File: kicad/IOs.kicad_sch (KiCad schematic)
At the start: 57 parts, among them J1 Screw_Terminal_01x04, J2 Screw_Terminal_01x04, J3 Screw_Terminal_01x04, J4 Screw_Terminal_01x04, J5 Screw_Terminal_01x04, J6 Screw_Terminal_01x04, Q1 BSS306NH, Q2 BSS306NH, Q3 BSS306NH, Q4 BSS306NH, Q5 BSS306NH, Q6 BSS306NH, SW2 SW_Push, SW3 SW_Push, SW4 SW_Push, U1 IX4340NE, U2 IX4340NE, U3 IX4340NE

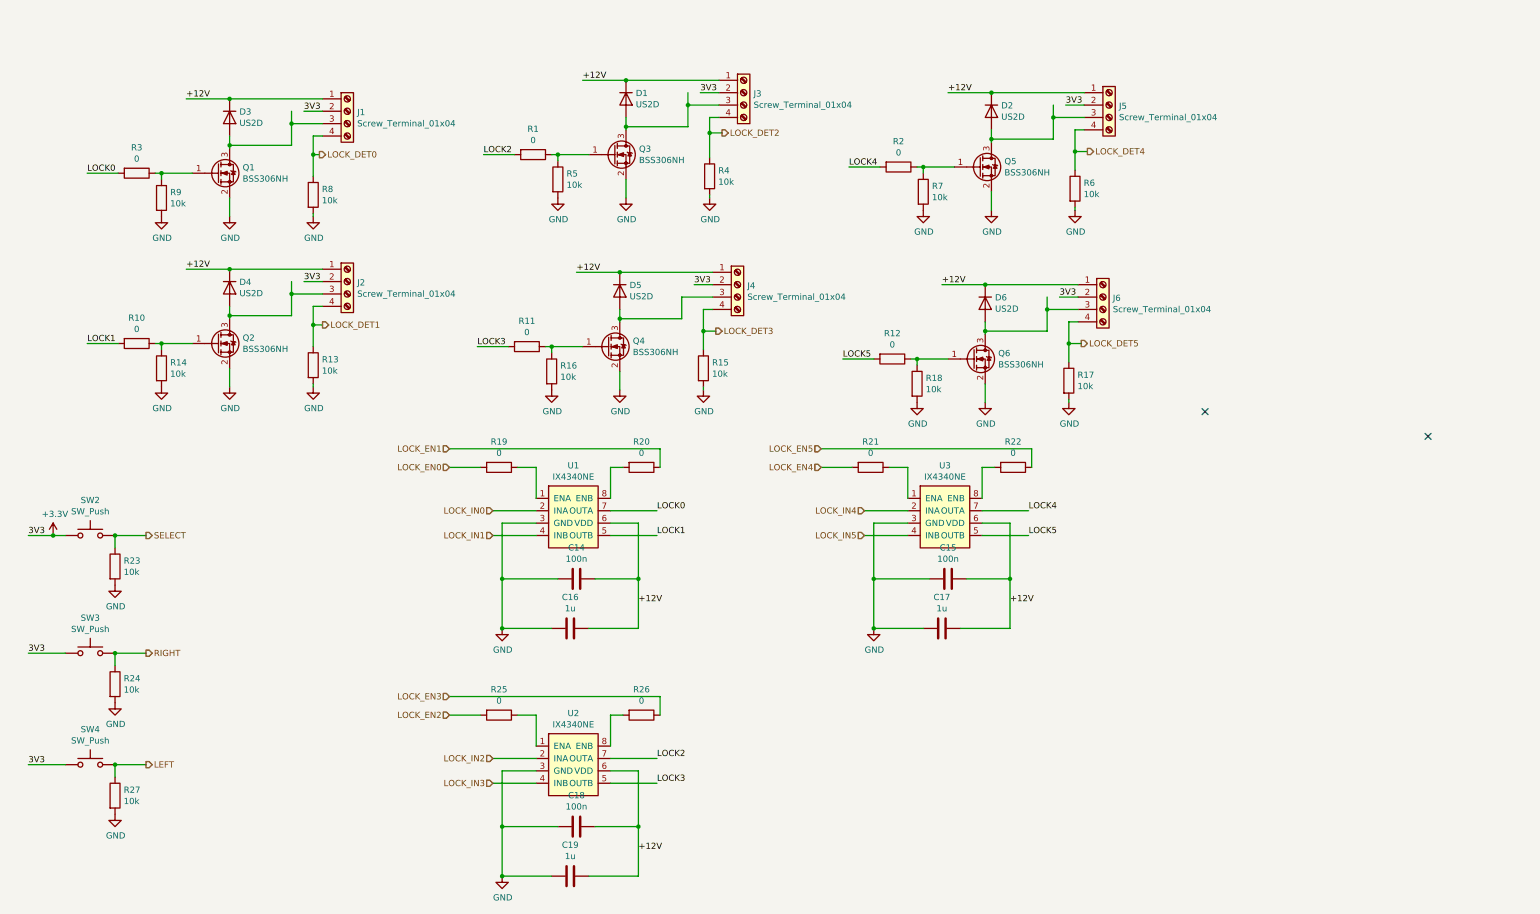
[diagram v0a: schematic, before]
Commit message: Update PCB with IO expander
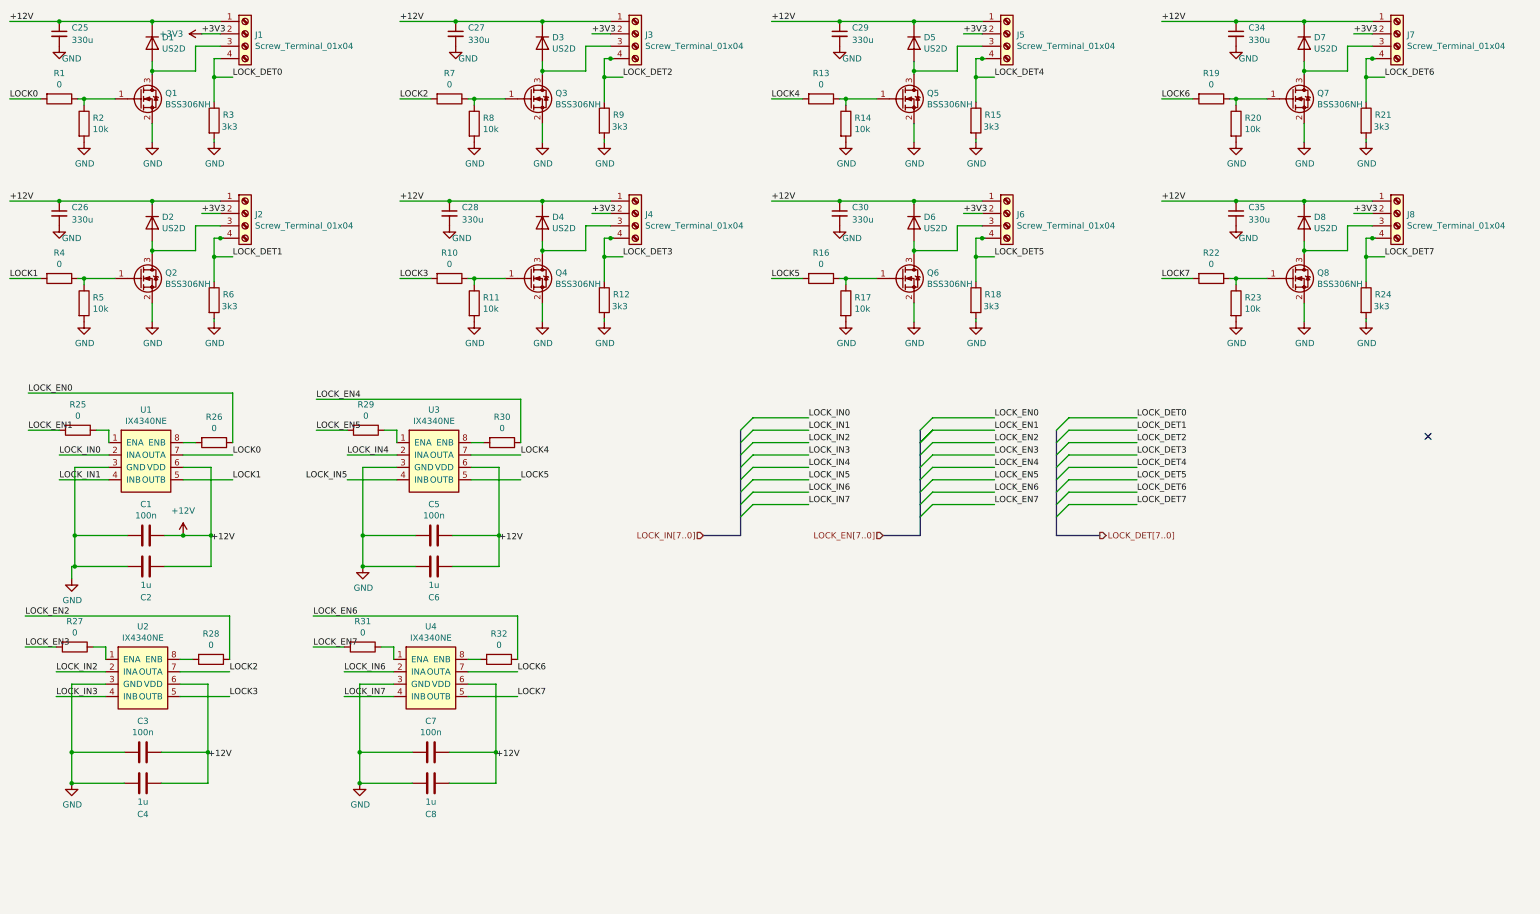
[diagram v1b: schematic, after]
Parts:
- removed C15, C18: 100n, Capacitor_SMD:C_0805_2012Metric_Pad1.15x1.40mm_HandSolder, symbol Device:C
- removed C17, C19: 1u, Capacitor_SMD:C_0805_2012Metric_Pad1.15x1.40mm_HandSolder, symbol Device:C
- removed D1: US2D, Diode_SMD:D_SMB, symbol Device:D
- removed R1, R2, R25, R26: 0, Resistor_SMD:R_0805_2012Metric_Pad1.15x1.40mm_HandSolder, symbol Device:R
- removed SW2, SW3, SW4: SW_Push, Connector_PinHeader_2.54mm:PinHeader_1x02_P2.54mm_Vertical, symbol Switch:SW_Push
- added C25, C26, C27, C28, C29, C30, C34, C35: 330u, Capacitor_THT:CP_Radial_D8.0mm_P3.50mm, symbol Device:C_Small
- added C3, C5, C7: 100n, Capacitor_SMD:C_0805_2012Metric_Pad1.18x1.45mm_HandSolder, symbol Device:C
- added C4, C6, C8: 1u, Capacitor_SMD:C_0805_2012Metric_Pad1.18x1.45mm_HandSolder, symbol Device:C
- added D3, D7, D8: US2D, Diode_SMD:D_SMB, symbol Device:D
- added J7, J8: Screw_Terminal_01x04, Connector_PinHeader_2.54mm:PinHeader_2x02_P2.54mm_Vertical, symbol Connector:Screw_Terminal_01x04
- added Q7, Q8: BSS306NH, Package_TO_SOT_SMD:SOT-23, symbol Device:Q_NMOS_GSD
- added R19, R28, R29, R30, R31, R32: 0, Resistor_SMD:R_0805_2012Metric_Pad1.20x1.40mm_HandSolder, symbol Device:R
- added R20, R8: 10k, Resistor_SMD:R_0805_2012Metric_Pad1.20x1.40mm_HandSolder, symbol Device:R
- added R9: 3k3, Resistor_SMD:R_0805_2012Metric_Pad1.20x1.40mm_HandSolder, symbol Device:R
- added U4: IX4340NE, Package_SO:SOIC-8-1EP_3.9x4.9mm_P1.27mm_EP2.29x3mm, symbol mosfet_drivers:IX4340NE
- C1: renamed from C14; footprint Capacitor_SMD:C_0805_2012Metric_Pad1.15x1.40mm_HandSolder -> Capacitor_SMD:C_0805_2012Metric_Pad1.18x1.45mm_HandSolder
- C2: renamed from C16; footprint Capacitor_SMD:C_0805_2012Metric_Pad1.15x1.40mm_HandSolder -> Capacitor_SMD:C_0805_2012Metric_Pad1.18x1.45mm_HandSolder
- R1: renamed from R3; footprint Resistor_SMD:R_0805_2012Metric_Pad1.15x1.40mm_HandSolder -> Resistor_SMD:R_0805_2012Metric_Pad1.20x1.40mm_HandSolder
- R10, R14, R17, R22, R23, R5: footprint Resistor_SMD:R_0805_2012Metric_Pad1.15x1.40mm_HandSolder -> Resistor_SMD:R_0805_2012Metric_Pad1.20x1.40mm_HandSolder
- R11: value 0 -> 10k; footprint Resistor_SMD:R_0805_2012Metric_Pad1.15x1.40mm_HandSolder -> Resistor_SMD:R_0805_2012Metric_Pad1.20x1.40mm_HandSolder
- R12, R21: value 0 -> 3k3; footprint Resistor_SMD:R_0805_2012Metric_Pad1.15x1.40mm_HandSolder -> Resistor_SMD:R_0805_2012Metric_Pad1.20x1.40mm_HandSolder
- R13, R16, R27, R4, R7: value 10k -> 0; footprint Resistor_SMD:R_0805_2012Metric_Pad1.15x1.40mm_HandSolder -> Resistor_SMD:R_0805_2012Metric_Pad1.20x1.40mm_HandSolder
- R15, R18, R24, R6: value 10k -> 3k3; footprint Resistor_SMD:R_0805_2012Metric_Pad1.15x1.40mm_HandSolder -> Resistor_SMD:R_0805_2012Metric_Pad1.20x1.40mm_HandSolder
- R2: renamed from R9; footprint Resistor_SMD:R_0805_2012Metric_Pad1.15x1.40mm_HandSolder -> Resistor_SMD:R_0805_2012Metric_Pad1.20x1.40mm_HandSolder
- R25: renamed from R19; footprint Resistor_SMD:R_0805_2012Metric_Pad1.15x1.40mm_HandSolder -> Resistor_SMD:R_0805_2012Metric_Pad1.20x1.40mm_HandSolder
- R26: renamed from R20; footprint Resistor_SMD:R_0805_2012Metric_Pad1.15x1.40mm_HandSolder -> Resistor_SMD:R_0805_2012Metric_Pad1.20x1.40mm_HandSolder
- R3: renamed from R8; value 10k -> 3k3; footprint Resistor_SMD:R_0805_2012Metric_Pad1.15x1.40mm_HandSolder -> Resistor_SMD:R_0805_2012Metric_Pad1.20x1.40mm_HandSolder
- U1, U2, U3: footprint mosfet_drivers:IX4340NE -> Package_SO:SOIC-8-1EP_3.9x4.9mm_P1.27mm_EP2.29x3mm
- renumbered D3 to D1
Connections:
- net LEFT is gone; now on an unnamed net: R27.1
- net +12V: now also C25.1, C26.1, C27.1, C28.1, C29.1, C3.1, C30.1, C34.1, C35.1, C4.1, C5.1, C6.1, C7.1, C8.1, D3.1 (K), D7.1 (K), D8.1 (K), J7.1 (Pin_1), J8.1 (Pin_1), U4.6 (VDD)
- net +3V3: now also J7.2 (Pin_2), J8.2 (Pin_2)
- net GND: now also R11.2, R12.2, R21.2, C25.2, C26.2, C27.2, C28.2, C29.2, C3.2, C30.2, C34.2, C35.2, C4.2, C5.2, C6.2, C7.2, C8.2, Q7.2 (S), Q8.2 (S), R20.2, R8.2, R9.2, U4.3 (GND); no longer R13.2, R16.2, R27.2, R4.2, R7.2
- net LOCK1: now also R4.2; no longer R10.2
- net LOCK2: now also R7.2
- net LOCK3: now also R10.2; no longer R11.2
- net LOCK4: now also R13.2
- net LOCK5: now also R16.2; no longer R12.2
- net LOCK_DET1: now also R6.1; no longer R13.1
- net LOCK_DET2: now also R9.1; no longer R4.1
- net LOCK_DET3: now also R12.1; no longer R15.1
- net LOCK_DET4: now also R15.1; no longer R6.1
- net LOCK_DET5: now also R18.1; no longer R17.1
- net LOCK_EN0: now also R26.1; no longer R25.2
- net LOCK_EN1: now also R25.2; no longer R26.1
- net LOCK_EN2: now also R28.1
- net LOCK_EN3: now also R27.2
- net LOCK_EN4: now also R30.1; no longer R21.2
- net LOCK_EN5: now also R29.2; no longer R22.1
- net at U2.8 (ENB): now also R28.2
- net at U3.1 (ENA): now also R29.1; no longer R21.1
- net at U3.8 (ENB): now also R30.2; no longer R22.2
- net at J2.3 (Pin_3), Q2.3 (D): now also D2.2 (A); no longer D4.2 (A)
- net at J3.3 (Pin_3), Q3.3 (D): now also D3.2 (A)
- net at Q3.1 (G): now also R7.1, R8.1; no longer R5.1
- net at J4.3 (Pin_3), Q4.3 (D): now also D4.2 (A); no longer D5.2 (A)
- net at Q4.1 (G), R11.1: now also R10.1; no longer R16.1
- net at Q5.1 (G): now also R13.1, R14.1; no longer R7.1
- net at J5.3 (Pin_3), Q5.3 (D): now also D5.2 (A); no longer D2.2 (A)
- net RIGHT renamed LOCK_DET7
- net LOCK_DET7: now also J8.4 (Pin_4)
- net SELECT: no longer names the net of R23.1
- net SELECT: now also R22.1, Q8.1 (G)
- new net: Q7.1 (G), R19.1, R20.1
- new net: D7.2 (A), J7.3 (Pin_3), Q7.3 (D)
- new net: R32.2, U4.8 (ENB)
- new net: Q6.1 (G), R16.1, R17.1
- new net: R31.1, U4.1 (ENA)
- new net: D8.2 (A), J8.3 (Pin_3), Q8.3 (D)
- new net: Q2.1 (G), R4.1, R5.1
- new net LOCK6: R19.2, U4.7 (OUTA)
- new net LOCK7: R22.2, U4.5 (OUTB)
- new net LOCK_DET6: J7.4 (Pin_4), R21.1
- new net LOCK_EN6: R32.1
- new net LOCK_EN7: R31.2
- new net LOCK_IN6: U4.2 (INA)
- new net LOCK_IN7: U4.4 (INB)
- no-connect marks 2 -> 1
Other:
- moved on the sheet: C1, C2, D1, J1, Q1, R1, R2, R25, R26, R3, U1

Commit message: Fix remaining DRC + ERC, ready for manufacturing
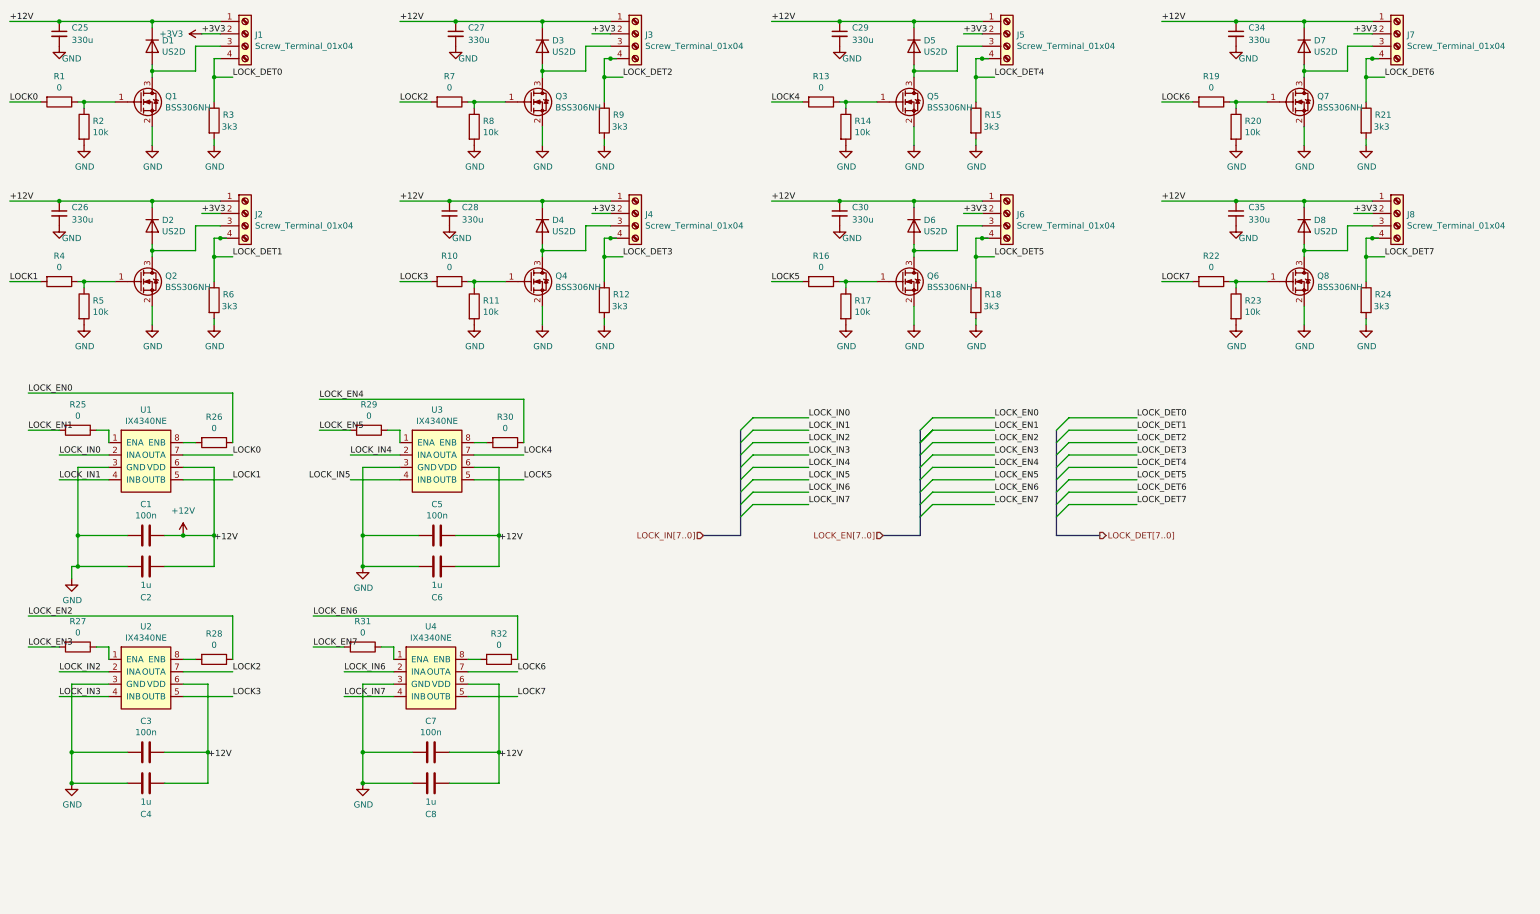
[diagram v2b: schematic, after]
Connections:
- no-connect marks 1 -> 0
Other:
- moved on the sheet: C3, C4, C5, C6, D1, D2, D3, D4, D5, D6, D7, D8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
